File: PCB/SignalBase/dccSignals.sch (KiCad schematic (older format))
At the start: 29 parts, among them J2 AVR-ISP-6, J3 leds, J4 leds, J5 leds, J6 leds, SW1 SW_DIP_x08, U3 ULN2803A, U4 ULN2803A, Y1 Resonator

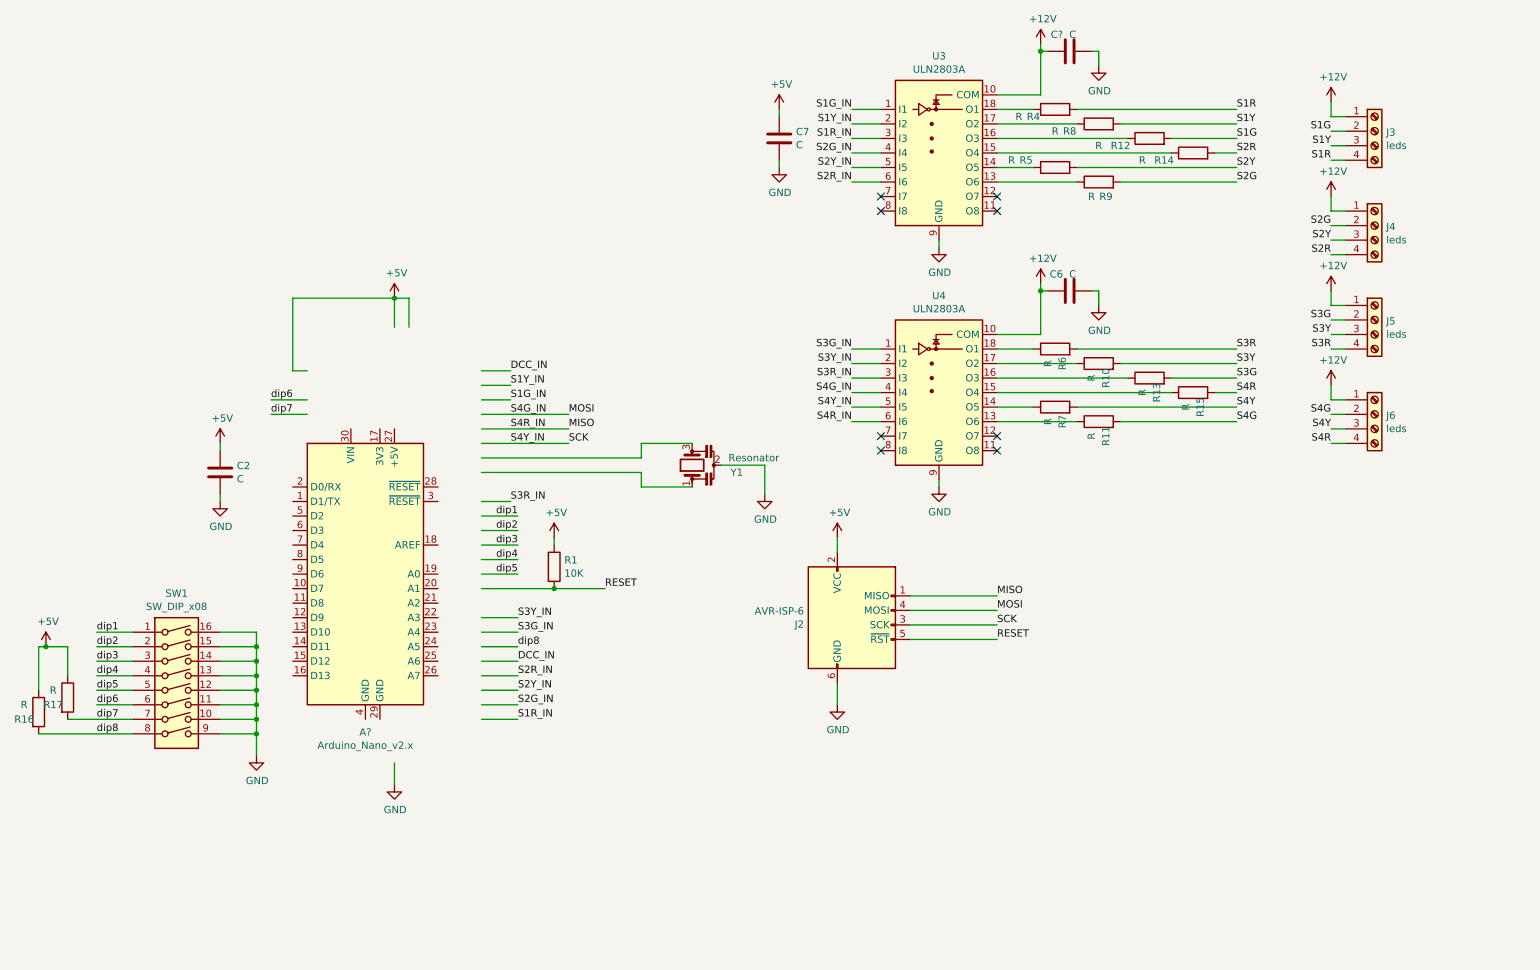
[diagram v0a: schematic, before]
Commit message: added signal base, fixed vias on mosgfet modules
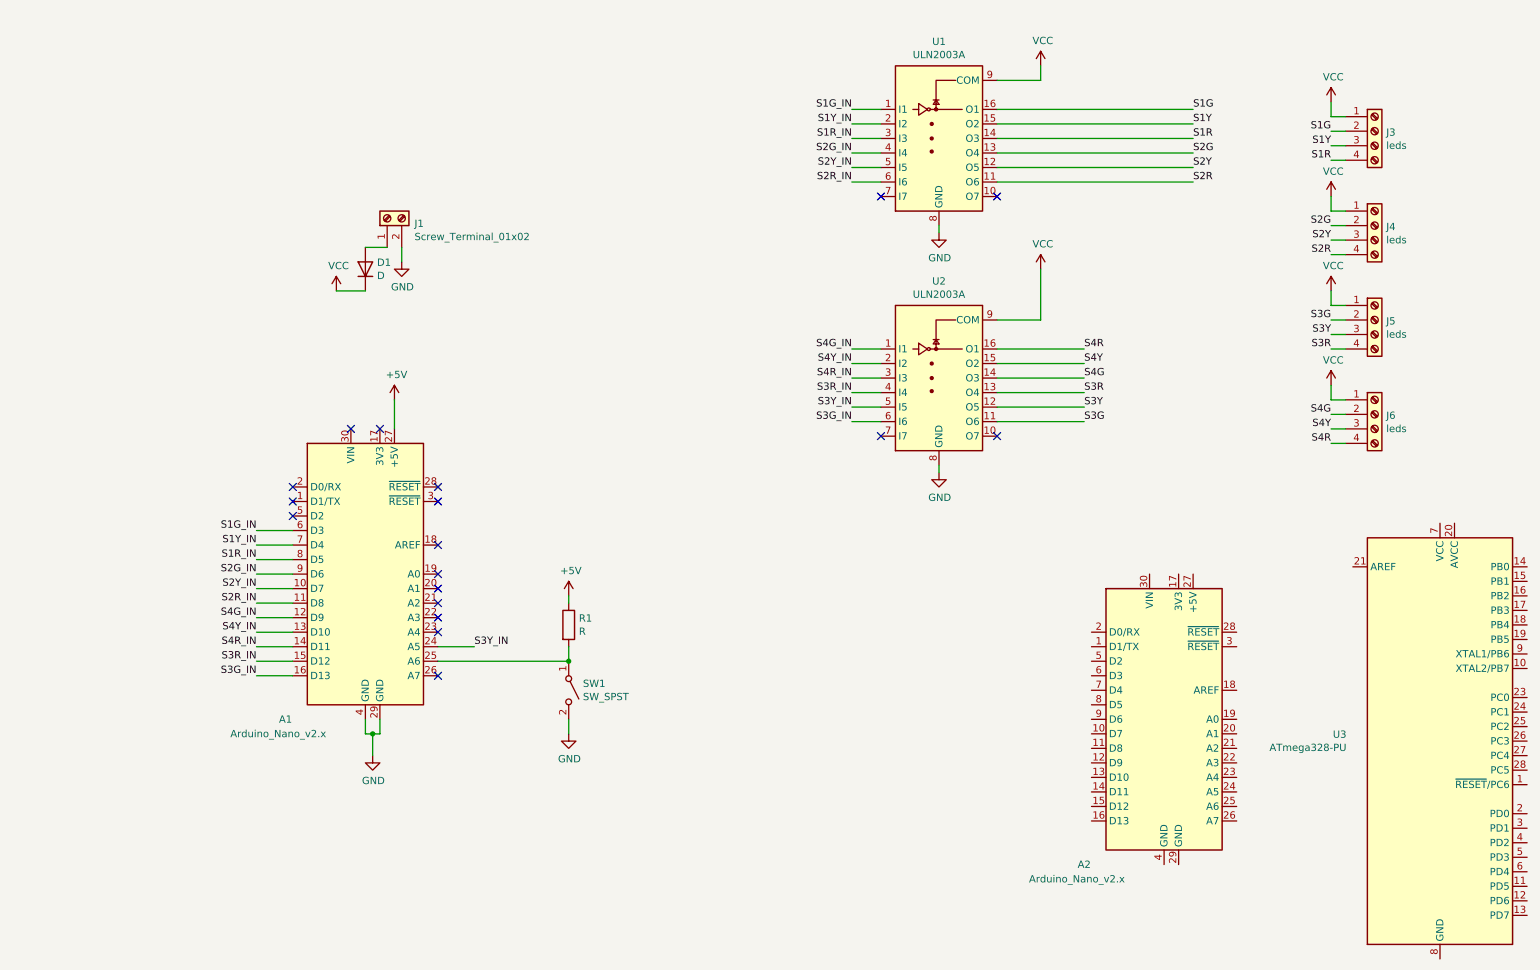
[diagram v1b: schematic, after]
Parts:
- removed C2, C6, C7, C?: C, Capacitor_SMD:C_0805_2012Metric, symbol Device:C
- removed J2: AVR-ISP-6, Connector_PinHeader_1.27mm:PinHeader_2x03_P1.27mm_Vertical, symbol Connector:AVR-ISP-6
- removed R10, R11, R12, R13, R14, R15, R16, R17, R4, R5, R6, R7, R8, R9: R, Resistor_SMD:R_0805_2012Metric, symbol Device:R
- removed SW1: SW_DIP_x08, Button_Switch_SMD:SW_DIP_SPSTx08_Slide_Omron_A6S-810x_W8.9mm_P2.54mm, symbol Switch:SW_DIP_x08
- removed U3, U4: ULN2803A, Package_SO:SOIC-18W_7.5x11.6mm_P1.27mm, symbol Transistor_Array:ULN2803A
- removed Y1: Resonator, Crystal:Resonator_SMD-3Pin_7.2x3.0mm_HandSoldering, symbol Device:Resonator
- added A2: Arduino_Nano_v2.x, Module:Arduino_Nano, symbol MCU_Module:Arduino_Nano_v2.x
- added D1: D, Diode_THT:D_DO-34_SOD68_P7.62mm_Horizontal, symbol Device:D
- added J1: Screw_Terminal_01x02, TerminalBlock_Phoenix:TerminalBlock_Phoenix_MKDS-1,5-2-5.08_1x02_P5.08mm_Horizontal, symbol Connector:Screw_Terminal_01x02
- added SW1: SW_SPST, Button_Switch_THT:SW_PUSH_6mm_H4.3mm, symbol Switch:SW_SPST
- added U1, U2: ULN2003A, Package_DIP:DIP-16_W7.62mm, symbol Transistor_Array:ULN2003A
- added U3: ATmega328-PU, Package_DIP:DIP-28_W7.62mm, symbol MCU_Microchip_ATmega:ATmega328-PU
- R1: value 10K -> R; footprint Resistor_SMD:R_0805_2012Metric -> Resistor_THT:R_Axial_DIN0207_L6.3mm_D2.5mm_P7.62mm_Horizontal
- gave numbers to parts that had none: 1
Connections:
- net labels added: VCC
- net labels removed: +12V, DCC_IN, MISO, MOSI, RESET, SCK, dip1, dip2, dip3, dip4, dip5, dip6, dip7, dip8
- wire segments 148 -> 75
- no-connect marks 8 -> 18
